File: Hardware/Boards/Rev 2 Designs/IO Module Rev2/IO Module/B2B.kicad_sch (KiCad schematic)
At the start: 2 parts, among them J2 LSHM-130-XX.X-XXX-DV-A-S-K-XX, J3 LSHM-130-XX.X-XXX-DV-A-S-K-XX

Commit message: Rev 2 IO module complete
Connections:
- net HDMI_D2_P is gone; now on net GND: J3.34
- net MBUS_D12 is gone; now on net MBUS_D8: J2.22
- net MBUS_D13 is gone; now on net MBUS_D7: J2.24
- net MBUS_D14 is gone; now on net MBUS_D6: J2.26
- net CAM_LED_EN: now also J2.04; no longer J3.03
- net CAM_PWR_EN: now also J2.02; no longer J3.01
- net FIFO_BE0: now also J2.44; no longer J2.33
- net FIFO_BE1: now also J2.42; no longer J2.31
- net FIFO_CLK: now also J2.29; no longer J2.35
- net FIFO_D0: now also J2.13; no longer J2.51
- net FIFO_D1: now also J2.15; no longer J2.49
- net FIFO_D10: now also J2.35; no longer J2.42
- net FIFO_D11: now also J2.37; no longer J2.40
- net FIFO_D12: now also J2.52; no longer J2.38
- net FIFO_D13: now also J2.50; no longer J2.36
- net FIFO_D14: now also J2.48; no longer J2.34
- net FIFO_D15: now also J2.46; no longer J2.32
- net FIFO_D2: now also J2.17; no longer J2.47
- net FIFO_D3: now also J2.19; no longer J2.45
- net FIFO_D4: now also J2.21; no longer J2.43
- net FIFO_D5: now also J2.23; no longer J2.41
- net FIFO_D6: now also J2.25; no longer J2.39
- net FIFO_D7: now also J2.27; no longer J2.37
- net FIFO_D8: now also J2.31; no longer J2.46
- net FIFO_D9: now also J2.33; no longer J2.44
- net FPGA_I2C_SCL: now also J3.19; no longer J2.02
- net FPGA_I2C_SDA: now also J3.17; no longer J2.04
- net FT600_OE: now also J2.47; no longer J3.27
- net FT600_RD: now also J2.45; no longer J2.50
- net FT600_RST: now also J2.49; no longer J3.25
- net FT600_RXE: now also J2.41; no longer J3.29
- net FT600_TXE: now also J2.39; no longer J3.31
- net FT600_WAKEUP: now also J2.51; no longer J3.23
- net FT600_WR: now also J2.43; no longer J2.52
- net GND: now also J2.14, J2.40; no longer J2.28, J2.29, J2.30, J2.48, J3.05, J3.07, J3.09, J3.11, J3.13, J3.15, J3.17, J3.19, J3.33, J3.38, J3.44, J3.50, J3.56, J3.58
- net MBUS_D0: now also J2.38; no longer J2.13
- net MBUS_D1: now also J2.36; no longer J2.15
- net MBUS_D11: now also J2.16; no longer J2.20
- net MBUS_D2: now also J2.34; no longer J2.17
- net MBUS_D3: now also J2.32; no longer J2.19
- net MBUS_D4: now also J2.30; no longer J2.21
- net MBUS_D5: now also J2.28; no longer J2.23
- net MBUS_D6: no longer J2.25
- net MBUS_D7: no longer J2.27
- net MBUS_D8: no longer J2.14
- net MBUS_D9: now also J2.20; no longer J2.16
- net USB_SYSMON_D_N: now also J2.08; no longer J2.10
- net USB_SYSMON_D_P: now also J2.10; no longer J2.08
- net HDMI_CEC renamed HDMI_DB7
- net HDMI_CLK_N renamed HDMI_DR5
- net HDMI_CLK_P renamed HDMI_DR4
- net HDMI_D0_N renamed HDMI_DR2
- net HDMI_D0_P renamed HDMI_DR1
- net HDMI_D1_N renamed HDMI_DE
- net HDMI_D1_P renamed HDMI_HSYNC
- net HDMI_D2_N renamed HDMI_IDCLK
- net HDMI_EQ_SEL renamed HDMI_DG6
- net HDMI_HPD_SRC renamed HDMI_DG4
- net HDMI_I2C_EN renamed HDMI_DG7
- net HDMI_I2C_SRC_EN renamed HDMI_DB6
- net HDMI_OE renamed HDMI_DG2
- net HDMI_PRE_SEL renamed HDMI_DG5
- net HDMI_SCL_SRC renamed HDMI_DB4
- net HDMI_SDA_SRC renamed HDMI_DB5
- net HDMI_SEL renamed HDMI_DG3
- net HDMI_SLEW_CTL renamed HDMI_DG1
- net TPD5_EN renamed HDMI_DG0
- new net HDMI_DB0: J3.27
- new net HDMI_DB1: J3.29
- new net HDMI_DB2: J3.31
- new net HDMI_DB3: J3.33
- new net HDMI_DR0: J3.44
- new net HDMI_DR3: J3.50
- new net HDMI_DR6: J3.56
- new net HDMI_DR7: J3.58
- new net HDMI_INT: J3.23
- new net HDMI_MCLK: J3.15
- new net HDMI_RST: J3.25
- new net HDMI_SCK: J3.13
- new net HDMI_SD0_DL0: J3.09
- new net HDMI_SD1_DR1: J3.07
- new net HDMI_SD2_DL1: J3.05
- new net HDMI_SD3_DR2: J3.03
- new net HDMI_SPDIF: J3.01
- new net HDMI_VSYNC: J3.38
- new net HDMI_WS_DR0: J3.11
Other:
- note removed: "FPGA GTY XCVR (1V2)"
- note removed: "FPGA GTY XCVR (1V2) OR FPGA 1V8 LVDS"
- moved on the sheet: J3

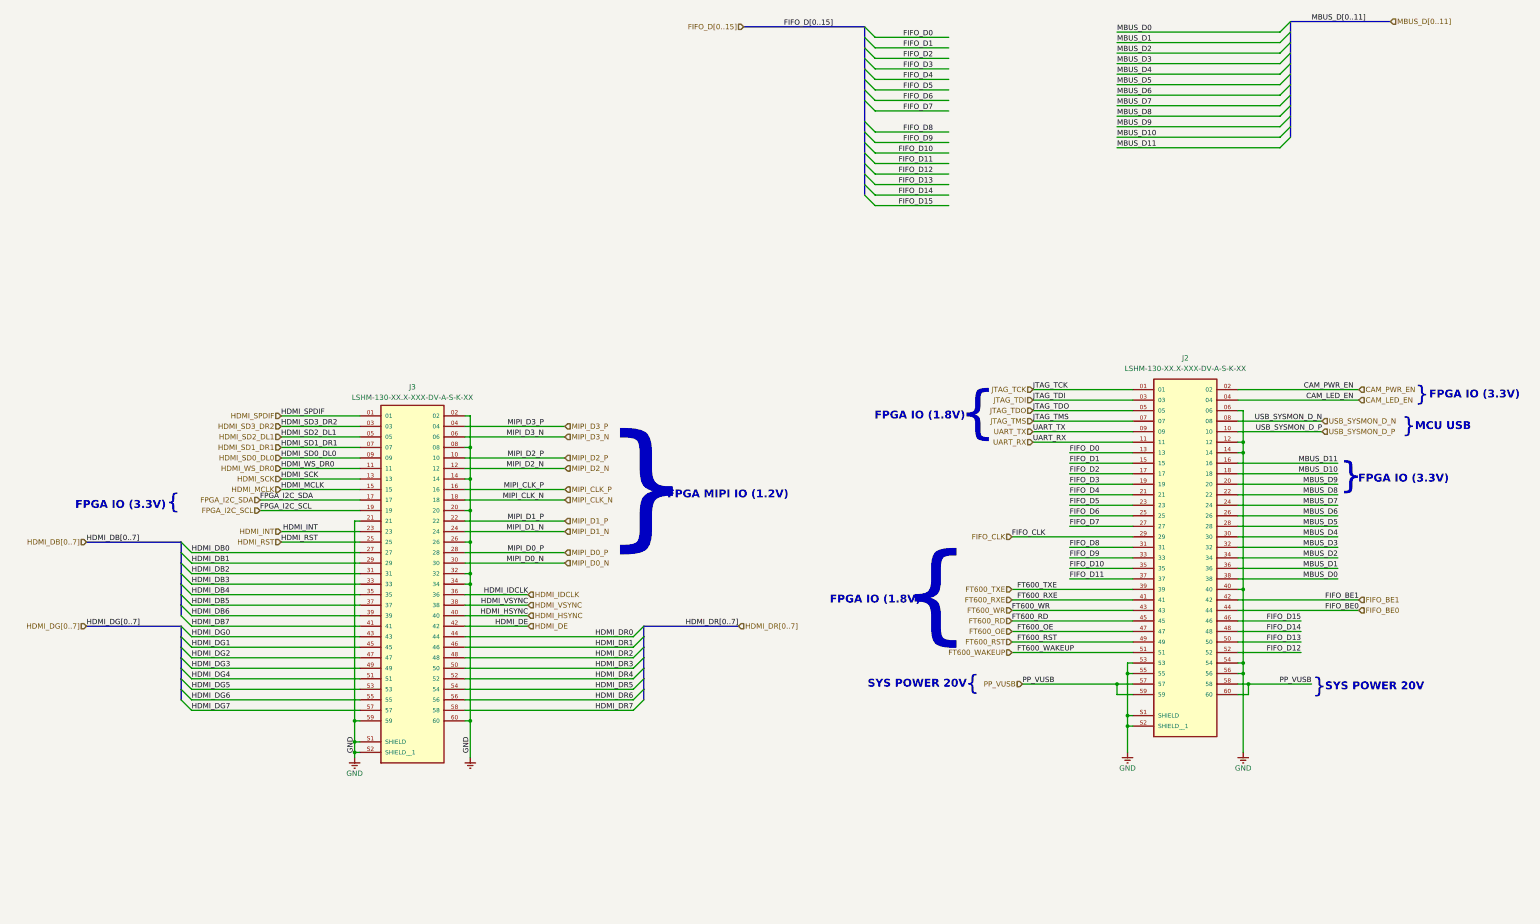
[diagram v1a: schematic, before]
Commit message: FPGA Module Rev 2 Layout Begun
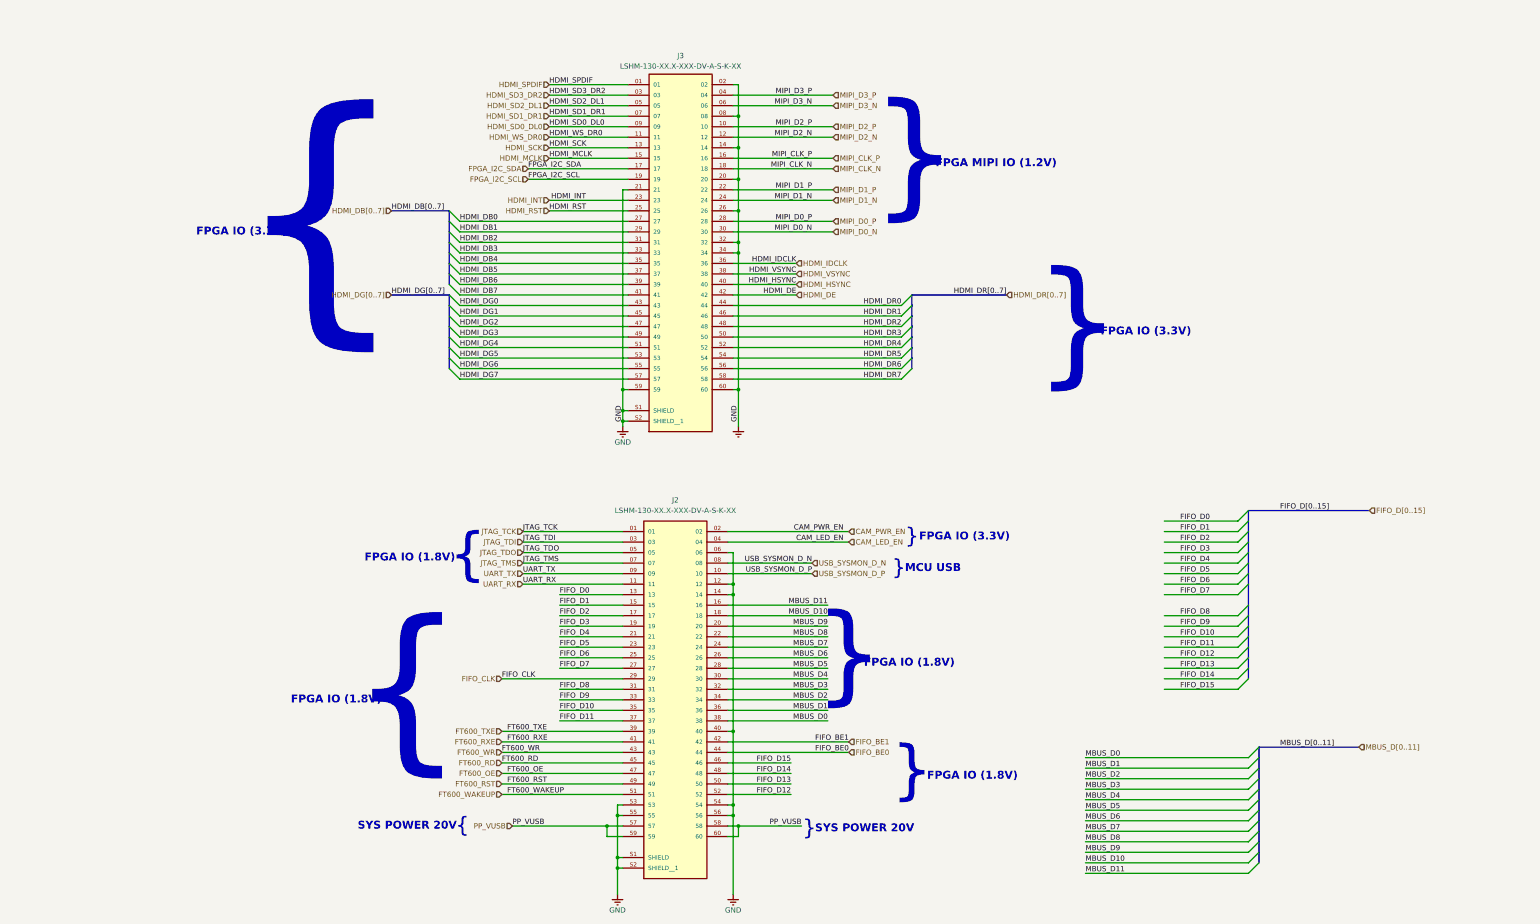
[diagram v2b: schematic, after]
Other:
- moved on the sheet: J2, J3
